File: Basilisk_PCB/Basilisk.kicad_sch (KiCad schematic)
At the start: 67 parts, among them J1 HUB75E, J2 Conn_01x04, J3 Barrel_Jack, J4 USB_C_Receptacle_USB2.0, Q1 S8050, Q2 S8050, SW1 IO0, SW2 RST, U1 AT25SF081-SSHD-X, U2 ESP32-WROOM-32D, U3 MLX90640, U4 TXS0108EPW, U5 TXS0108EPW, U6 AMS1117-3.3, U7 TPS54560BDDA, U8 FT231XS

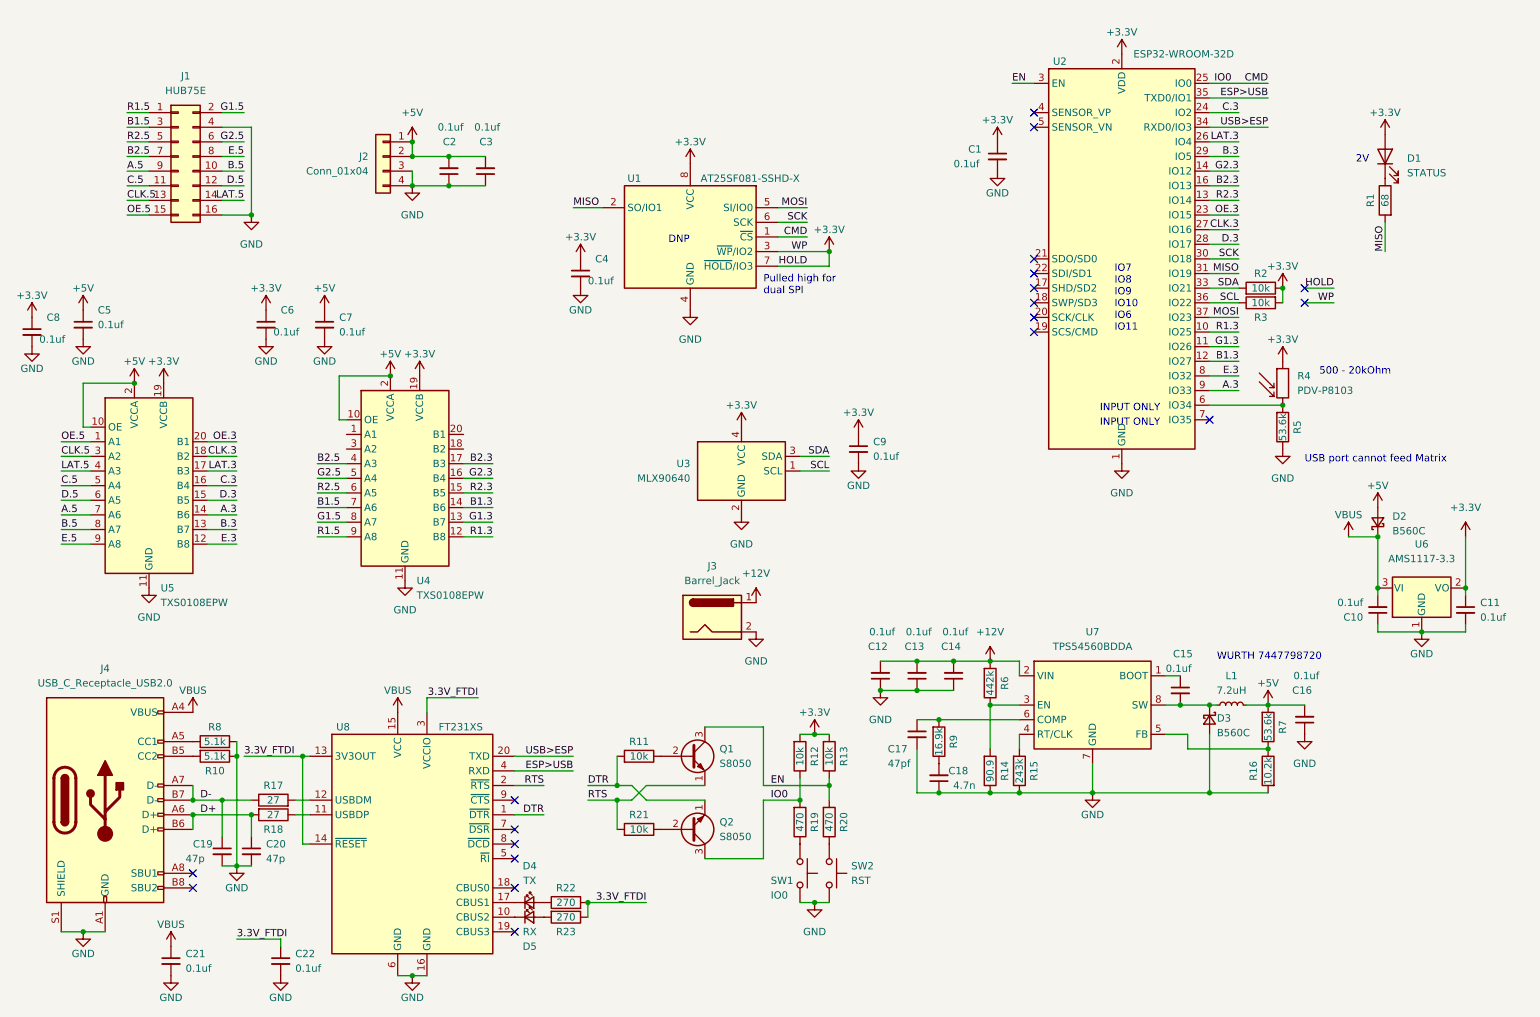
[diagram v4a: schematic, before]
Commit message: almost done routuing
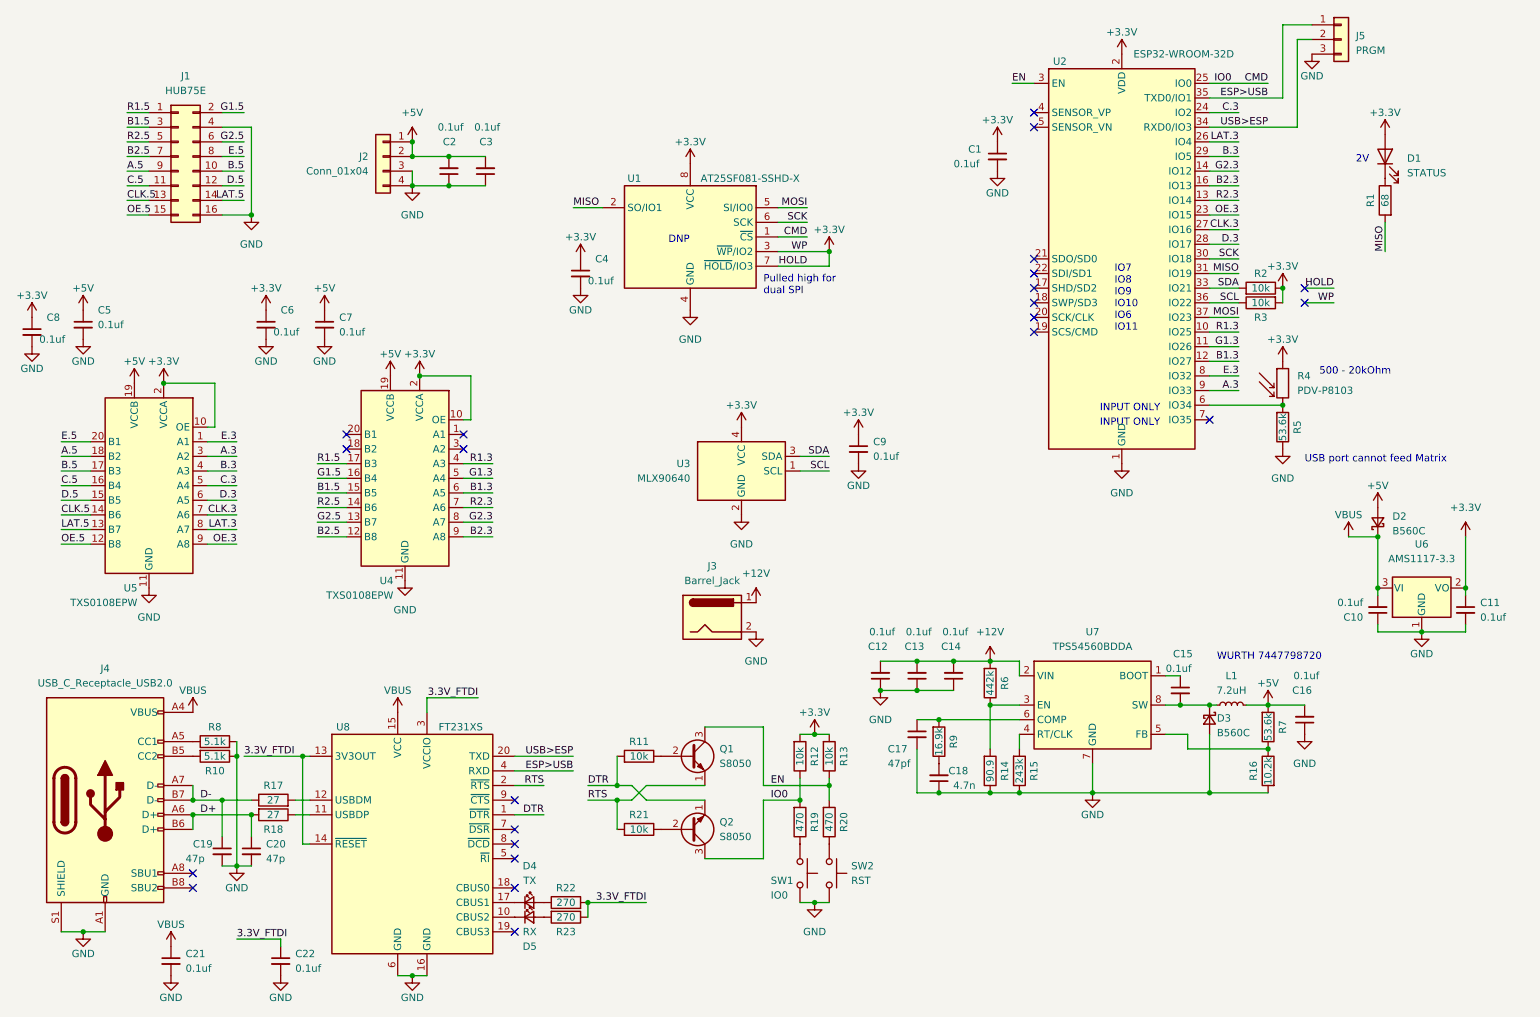
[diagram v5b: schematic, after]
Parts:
- added J5: PRGM, Connector_PinHeader_2.54mm:PinHeader_1x03_P2.54mm_Vertical, symbol Connector_Generic:Conn_01x03
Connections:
- net +3.3V: now also U4.10 (OE), U4.2 (VCCA), U5.10 (OE), U5.2 (VCCA); no longer U4.19 (VCCB), U5.19 (VCCB)
- net +5V: now also U4.19 (VCCB), U5.19 (VCCB); no longer U4.10 (OE), U4.2 (VCCA), U5.10 (OE), U5.2 (VCCA)
- net A.3: now also U5.3 (A2); no longer U5.14 (B6)
- net A.5: now also U5.18 (B2); no longer U5.7 (A6)
- net B.3: now also U5.4 (A3); no longer U5.13 (B7)
- net B.5: now also U5.17 (B3); no longer U5.8 (A7)
- net B1.3: now also U4.6 (A5); no longer U4.14 (B6)
- net B1.5: now also U4.15 (B5); no longer U4.7 (A6)
- net B2.3: now also U4.9 (A8); no longer U4.17 (B3)
- net B2.5: now also U4.12 (B8); no longer U4.4 (A3)
- net C.3: now also U5.5 (A4); no longer U5.16 (B4)
- net C.5: now also U5.16 (B4); no longer U5.5 (A4)
- net CLK.3: now also U5.7 (A6); no longer U5.18 (B2)
- net CLK.5: now also U5.14 (B6); no longer U5.3 (A2)
- net D.3: now also U5.6 (A5); no longer U5.15 (B5)
- net D.5: now also U5.15 (B5); no longer U5.6 (A5)
- net E.3: now also U5.1 (A1); no longer U5.12 (B8)
- net E.5: now also U5.20 (B1); no longer U5.9 (A8)
- net ESP>USB: now also J5.1 (Pin_1)
- net G1.3: now also U4.5 (A4); no longer U4.13 (B7)
- net G1.5: now also U4.16 (B4); no longer U4.8 (A7)
- net G2.3: now also U4.8 (A7); no longer U4.16 (B4)
- net G2.5: now also U4.13 (B7); no longer U4.5 (A4)
- net GND: now also J5.3 (Pin_3)
- net LAT.3: now also U5.8 (A7); no longer U5.17 (B3)
- net LAT.5: now also U5.13 (B7); no longer U5.4 (A3)
- net OE.3: now also U5.9 (A8); no longer U5.20 (B1)
- net OE.5: now also U5.12 (B8); no longer U5.1 (A1)
- net R1.3: now also U4.4 (A3); no longer U4.12 (B8)
- net R1.5: now also U4.17 (B3); no longer U4.9 (A8)
- net R2.3: now also U4.7 (A6); no longer U4.15 (B5)
- net R2.5: now also U4.14 (B6); no longer U4.6 (A5)
- net USB>ESP: now also J5.2 (Pin_2)
- no-connect marks 19 -> 23

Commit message: version 1.0
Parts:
- J3: symbol Connector:Barrel_Jack -> Connector:Barrel_Jack_Switch
- Q1, Q2: symbol Transistor_BJT:S8050 -> Device:Q_NPN_BEC
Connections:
- net DTR: now also Q2.2 (E); no longer Q2.1 (E)
- net GND: now also J3.3
- net RTS: now also Q1.2 (E); no longer Q1.1 (E)
- net at R21.1: now also Q2.1 (B); no longer Q2.2 (B)
- net at R11.1: now also Q1.1 (B); no longer Q1.2 (B)
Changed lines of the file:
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@@
   (junction (at 180.34 157.48) (diameter 0) (color 0 0 0 0)
   )
+  (junction (at 148.59 129.54) (diameter 0) (color 0 0 0 0)
+  )
   (junction (at 271.78 121.92) (diameter 0) (color 0 0 0 0)
   )
@@
     (stroke (width 0) (type default))
   )
+  (wire (pts (xy 148.59 127) (xy 148.59 129.54))
+    (stroke (width 0) (type default))
+  )
   (wire (pts (xy 72.39 107.95) (xy 77.47 107.95))
     (stroke (width 0) (type default))
@@
   (symbol (lib_id "Regulator_Switching:TPS54560BDDA") (at 207.01 142.24 0) (unit 1)
     (in_bom yes) (on_board yes) (dnp no) (fields_autoplaced)
-    (property "Reference" "U7" (at 207.01 129.54 0)
+    (property "Reference" "U7" (at 207.01 130.81 0)
       (effects (font (size 1.27 1.27)))
     )
-    (property "Value" "TPS54560BDDA" (at 207.01 132.08 0)
+    (property "Value" "TPS54560BDDA" (at 207.01 133.35 0)
       (effects (font (size 1.27 1.27)))
     )
@@
     )
   )
-  (symbol (lib_id "Connector:Barrel_Jack") (at 140.97 127 0) (unit 1)
+  (symbol (lib_id "Connector:Barrel_Jack_Switch") (at 140.97 127 0) (unit 1)
     (in_bom yes) (on_board yes) (dnp no) (fields_autoplaced)
     (property "Reference" "J3" (at 140.97 118.11 0)
@@
     (pin "1")
     (pin "2")
+    (pin "3")
     (instances
       (project "Basilisk"
@@
     )
   )
-  (symbol (lib_id "Transistor_BJT:S8050") (at 137.16 163.83 0) (mirror x) (unit 1)
+  (symbol (lib_id "Device:Q_NPN_BEC") (at 137.16 163.83 0) (mirror x) (unit 1)
     (in_bom yes) (on_board yes) (dnp no) (fields_autoplaced)
     (property "Reference" "Q2" (at 142.24 162.5599 0)
@@
       (effects (font (size 1.27 1.27)) (justify left))
     )
-    (property "Footprint" "Package_TO_SOT_SMD:SOT-23" (at 142.24 161.925 0)
-      (effects (font (size 1.27 1.27) italic) (justify left) hide)
+    (property "Footprint" "Package_TO_SOT_SMD:SOT-23" (at 142.24 166.37 0)
+      (effects (font (size 1.27 1.27)) hide)
     )
-    (property "Datasheet" "http://www.unisonic.com.tw/datasheet/S8050.pdf" (at 137.16 163.83 0)
-      (effects (font (size 1.27 1.27)) (justify left) hide)
+    (property "Datasheet" "~" (at 137.16 163.83 0)
+      (effects (font (size 1.27 1.27)) hide)
     )
     (pin "1")
@@
     )
   )
-  (symbol (lib_id "Transistor_BJT:S8050") (at 137.16 151.13 0) (unit 1)
+  (symbol (lib_id "Device:Q_NPN_BEC") (at 137.16 151.13 0) (unit 1)
     (in_bom yes) (on_board yes) (dnp no)
     (property "Reference" "Q1" (at 142.24 149.8599 0)
@@
       (effects (font (size 1.27 1.27)) (justify left))
     )
-    (property "Footprint" "Package_TO_SOT_SMD:SOT-23" (at 142.24 153.035 0)
-      (effects (font (size 1.27 1.27) italic) (justify left) hide)
+    (property "Footprint" "Package_TO_SOT_SMD:SOT-23" (at 142.24 148.59 0)
+      (effects (font (size 1.27 1.27)) hide)
     )
-    (property "Datasheet" "http://www.unisonic.com.tw/datasheet/S8050.pdf" (at 137.16 151.13 0)
-      (effects (font (size 1.27 1.27)) (justify left) hide)
+    (property "Datasheet" "~" (at 137.16 151.13 0)
+      (effects (font (size 1.27 1.27)) hide)
     )
     (pin "1")
